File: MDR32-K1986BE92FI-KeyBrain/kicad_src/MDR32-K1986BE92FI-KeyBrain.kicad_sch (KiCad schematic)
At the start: 33 parts, among them J3 USB_C_Receptacle_USB2.0_16P, J4 Conn_01x04, U1 AP2112K-3.3, U2 K1986BE92FI, U3 USBLC6-2SC6, U4 ProMicro, Y1 8MHz

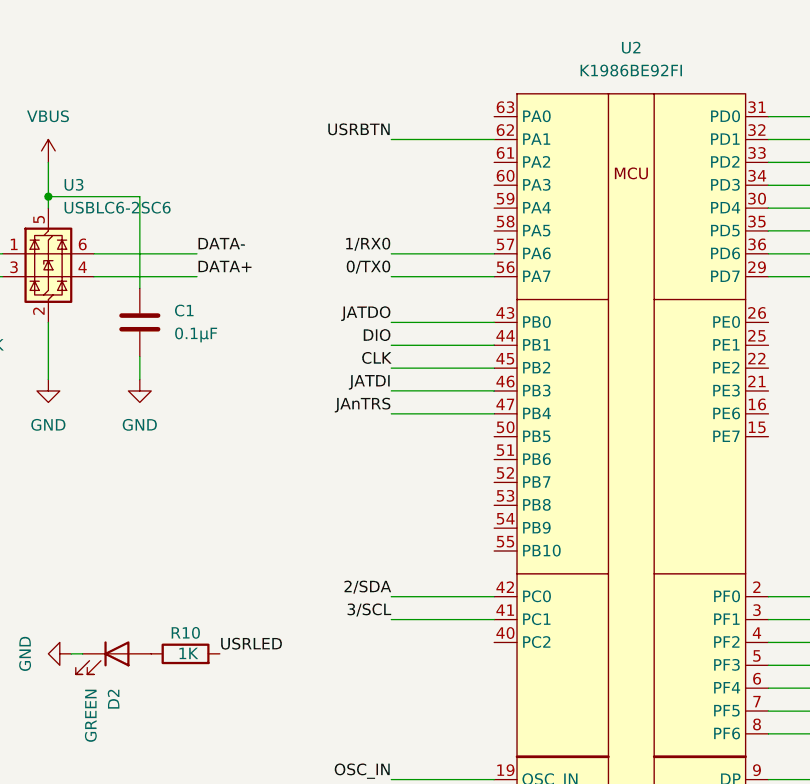
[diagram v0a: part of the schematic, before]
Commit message: MDR32-K1986BE92FI-KeyBrain: i2c pinout position
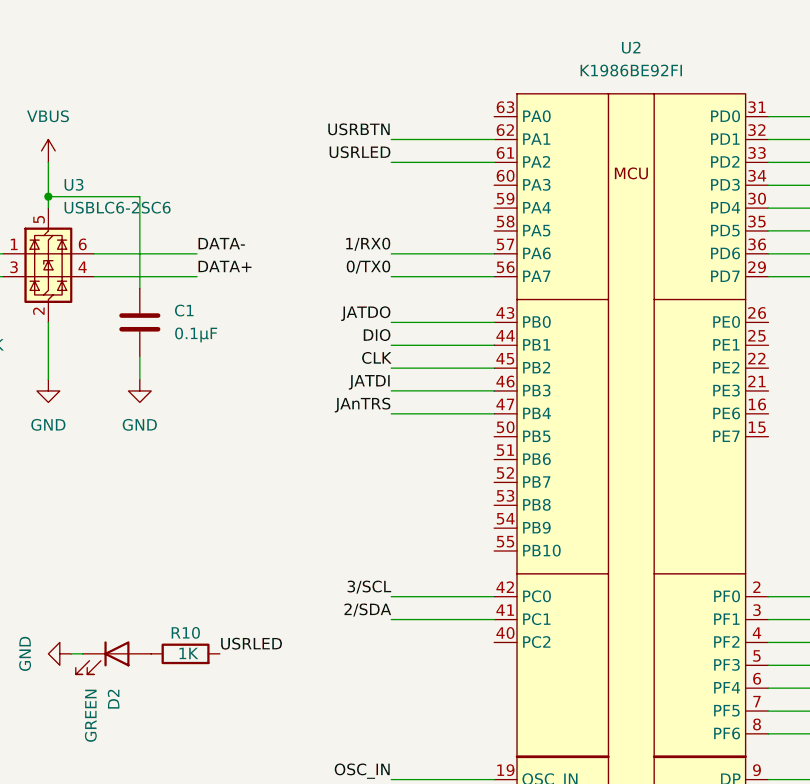
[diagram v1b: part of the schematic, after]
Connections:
- net 2/SDA: now also U2.41 (PC1); no longer U2.42 (PC0)
- net 3/SCL: now also U2.42 (PC0); no longer U2.41 (PC1)
- net USRLED: now also U2.61 (PA2)
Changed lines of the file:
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@@
 	(wire
 		(pts
+			(xy 113.03 31.75) (xy 124.46 31.75)
+		)
+		(stroke
+			(width 0)
+			(type default)
+		)
+	)
+	(wire
+		(pts
 			(xy 46.99 44.45) (xy 48.26 44.45)
 		)
@@
 		)
 	)
+	(label "USRLED"
+		(at 113.03 31.75 180)
+		(effects
+			(font
+				(size 1.27 1.27)
+			)
+			(justify right bottom)
+		)
+	)
 	(label "9{slash}RX1"
 		(at 167.64 26.67 0)
@@
 	)
 	(label "2{slash}SDA"
-		(at 113.03 80.01 180)
+		(at 113.03 82.55 180)
 		(effects
 			(font
@@
 	)
 	(label "3{slash}SCL"
-		(at 113.03 82.55 180)
+		(at 113.03 80.01 180)
 		(effects
 			(font

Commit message: MDR32-K1986BE92FI-KeyBrain: release unconnected
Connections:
- net 4: now also U2.58 (PA5)
- net 5: now also U2.60 (PA3)
- net 6: now also U2.61 (PA2)
- net 7: now also U2.63 (PA0)
- net USRLED: now also U2.59 (PA4); no longer U2.61 (PA2)
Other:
- note removed: "UNCONNECTED"
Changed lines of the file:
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@@
 	(paper "A4")
 	(rectangle
-		(start 161.925 117.475)
-		(end 193.04 135.89)
-		(stroke
-			(width 0)
-			(type dash)
-		)
-		(fill
-			(type none)
-		)
-	)
-	(rectangle
 		(start 167.64 87.63)
 		(end 180.34 96.52)
@@
 		)
 	)
-	(text "UNCONNECTED"
-		(exclude_from_sim no)
-		(at 178.308 112.522 0)
-		(effects
-			(font
-				(size 2.54 2.54)
-			)
-		)
-	)
 	(text "MODE Select"
 		(exclude_from_sim no)
@@
 	(wire
 		(pts
+			(xy 113.03 36.83) (xy 124.46 36.83)
+		)
+		(stroke
+			(width 0)
+			(type default)
+		)
+	)
+	(wire
+		(pts
 			(xy 121.92 130.81) (xy 124.46 130.81)
 		)
@@
 	(wire
 		(pts
+			(xy 113.03 39.37) (xy 124.46 39.37)
+		)
+		(stroke
+			(width 0)
+			(type default)
+		)
+	)
+	(wire
+		(pts
 			(xy 113.03 49.53) (xy 124.46 49.53)
 		)
@@
 	(wire
 		(pts
+			(xy 113.03 26.67) (xy 124.46 26.67)
+		)
+		(stroke
+			(width 0)
+			(type default)
+		)
+	)
+	(wire
+		(pts
 			(xy 243.84 138.43) (xy 257.81 138.43)
 		)
@@
 	(wire
 		(pts
+			(xy 113.03 34.29) (xy 124.46 34.29)
+		)
+		(stroke
+			(width 0)
+			(type default)
+		)
+	)
+	(wire
+		(pts
 			(xy 243.84 115.57) (xy 260.35 115.57)
 		)
@@
 		)
 	)
-	(label "7"
-		(at 168.91 129.54 0)
-		(effects
-			(font
-				(size 1.27 1.27)
-			)
-			(justify left bottom)
-		)
-	)
 	(label "D+"
 		(at 48.26 44.45 0)
@@
 		)
 	)
+	(label "7"
+		(at 113.03 26.67 180)
+		(effects
+			(font
+				(size 1.27 1.27)
+			)
+			(justify right bottom)
+		)
+	)
 	(label "JTAG_MODE1"
 		(at 167.64 90.17 0)
@@
 	)
 	(label "5"
-		(at 168.91 124.46 0)
+		(at 113.03 34.29 180)
 		(effects
 			(font
 				(size 1.27 1.27)
 			)
-			(justify left bottom)
+			(justify right bottom)
 		)
 	)
@@
 	)
 	(label "USRLED"
-		(at 113.03 31.75 180)
+		(at 113.03 36.83 180)
 		(effects
 			(font
@@
 		)
 	)
-	(label "DIO"
-		(at 181.61 129.54 270)
-		(effects
-			(font
-				(size 1.27 1.27)
-			)
-			(justify right bottom)
-		)
-	)
 	(label "OSC_IN"
 		(at 68.58 118.11 180)
@@
 		)
 	)
-	(label "DATA+"
-		(at 91.44 44.45 0)
+	(label "4"
+		(at 113.03 39.37 180)
 		(effects
 			(font
 				(size 1.27 1.27)
 			)
-			(justify left bottom)
+			(justify right bottom)
 		)
 	)
-	(label "6"
-		(at 168.91 127 0)
+	(label "DATA+"
+		(at 91.44 44.45 0)
 		(effects
 			(font
@@
 		)
 	)
-	(label "CLK"
-		(at 184.15 129.54 270)
-		(effects
-			(font
-				(size 1.27 1.27)
-			)
-			(justify right bottom)
-		)
-	)
 	(label "A1"
 		(at 167.64 34.29 0)
@@
 		)
 	)
+	(label "6"
+		(at 113.03 31.75 180)
+		(effects
+			(font
+				(size 1.27 1.27)
+			)
+			(justify right bottom)
+		)
+	)
 	(label "DATA+"
 		(at 170.18 100.33 0)
@@
 		)
 	)
-	(label "USRLED"
-		(at 177.8 124.46 0)
-		(effects
-			(font
-				(size 1.27 1.27)
-			)
-			(justify left bottom)
-		)
-	)
 	(label "JATDO"
 		(at 113.03 49.53 180)
@@
 		(effects
 			(font
-				(size 1.27 1.27)
-			)
-			(justify left bottom)
-		)
-	)
-	(label "4"
-		(at 168.91 121.92 0)
-		(effects
-			(font

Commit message: MDR32-K1986BE92FI-KeyBrain: fix errors
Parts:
- removed C12, C7: 10pF, Capacitor_SMD:C_0603_1608Metric, symbol MDR32-K1986BE92FI-DK:C
- added C2, C5: 10pF, Capacitor_SMD:C_0603_1608Metric, symbol Device:C
- renumbered C2 to C1, C1 to C4, C4 to C6, C5 to C7, C6 to C8, D4 to D1, D1 to D2, D2 to D3, F3 to F1, J3 to J1, J4 to J2, JP4 to JP1, JP5 to JP2, JP6 to JP3, R3 to R1, R11 to R10, R10 to R11, R4 to R2, R5 to R3, R6 to R4, R7 to R5, R8 to R6, R9 to R7, R1 to R8, R2 to R9, U3 to U2, U2 to U3
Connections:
- net 4: now also U3.29 (PD7); no longer U3.58 (PA5)
- net 5: now also U3.58 (PA5); no longer U3.60 (PA3)
- net 6: now also U3.36 (PD6); no longer U3.61 (PA2)
- net GND: now also C2.2, C5.2
- net OSC_IN: now also C2.1
- net OSC_OUT: now also C5.1
- no-connect marks 4 -> 19
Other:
- note added: "*1 Шунтирующие конденсаторы, обязательно около VCC, AVCC и AVCC1 *2 Активен режим JTAG_A, режим JTAG_B доступен только с манипуляцией *3 Опционально, но желательно * Не подключенные пины программно устанавливаются как цифровые и подтягиваются к + или - Делаем JTAG_B, окирпичить достаточно дорогой МК без возможности востановления не очень приятно. Аналоговые входы пока что не приоритетны."
- note removed: "*1 Шунтирующие конденсаторы, обязательно около VCC, AVCC и AVCC1 *2 Активен режим JTAG_A, режим JTAG_B доступен только с манипуляцией *3 Опционально, но желательно *? возможно лучше JTAG_B заменить на JTAG_A чтобы аналоговый порт был доступен целиком в таком случае, в случае глюков МК, не возможно будет его восстановить Делаем JTAG_B, окирпичить достаточно дорогой МК без возможности востановления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"

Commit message: MDR32-K1986BE92FI-KeyBrain: set jumper footprints
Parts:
- JP1, JP2, JP3: footprint (none) -> Jumper:SolderJumper-3_P1.3mm_Bridged12_RoundedPad1.0x1.5mm
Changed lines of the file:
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@@
 			)
 		)
-		(property "Footprint" ""
+		(property "Footprint" "Jumper:SolderJumper-3_P1.3mm_Bridged12_RoundedPad1.0x1.5mm"
 			(at 223.52 40.64 0)
 			(hide yes)
@@
 			)
 		)
-		(property "Footprint" ""
+		(property "Footprint" "Jumper:SolderJumper-3_P1.3mm_Bridged12_RoundedPad1.0x1.5mm"
 			(at 207.01 40.64 0)
 			(hide yes)
@@
 			)
 		)
-		(property "Footprint" ""
+		(property "Footprint" "Jumper:SolderJumper-3_P1.3mm_Bridged12_RoundedPad1.0x1.5mm"
 			(at 238.76 40.64 0)
 			(hide yes)

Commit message: MDR32-K1986BE92FI-KeyBrain: fix swd header
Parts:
- J2: footprint nrfmicro:connector_swd -> Connector_PinHeader_2.54mm:PinHeader_1x04_P2.54mm_Vertical
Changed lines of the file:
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@@
 			)
 		)
-		(property "Footprint" "nrfmicro:connector_swd"
+		(property "Footprint" "Connector_PinHeader_2.54mm:PinHeader_1x04_P2.54mm_Vertical"
 			(at 246.38 153.67 0)
 			(hide yes)
